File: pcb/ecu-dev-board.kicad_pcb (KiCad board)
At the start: 4 copper layers, 99.9 x 99.9 mm, 258 parts, among them IC201 MAX9924UAUB+, IC401 74HC14D-Q100,118, IC601 UCC28910DR, IC701 UCC27624DR, J101 MX23A18NF1, J102 39-30-1020, K501 Relay, Q201 MMBT2222A, Q501 MMBT2222A, Q502 MMBTA55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

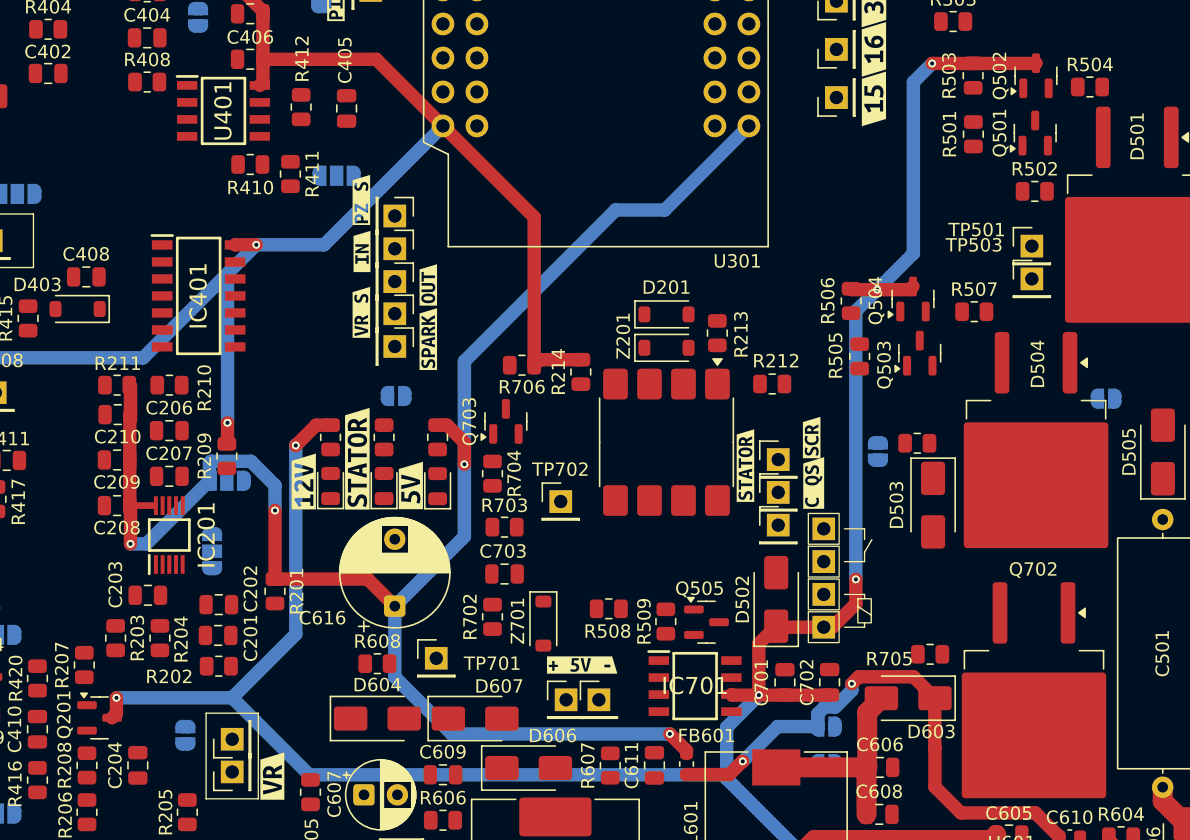
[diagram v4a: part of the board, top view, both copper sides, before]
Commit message: power aux connections
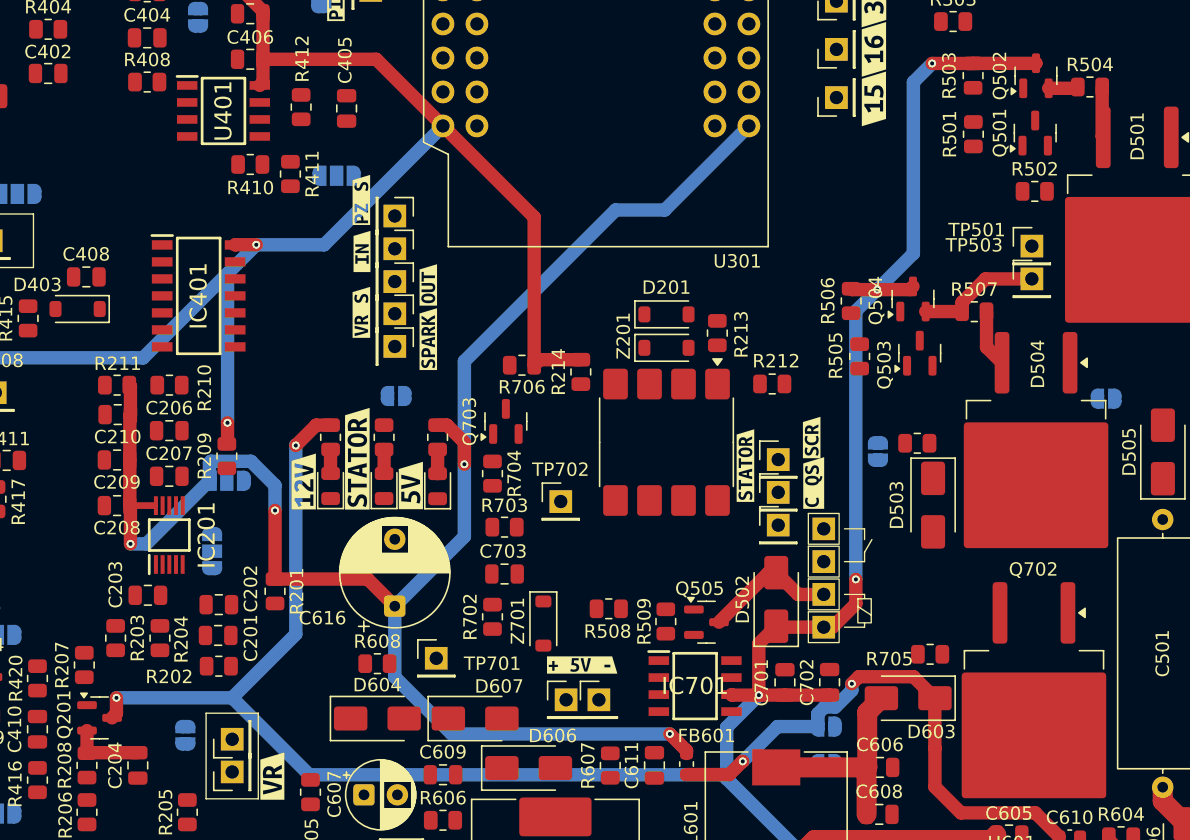
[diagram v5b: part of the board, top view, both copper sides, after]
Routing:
- net Net-(D502-A): track 0.00 -> 10.0 mm
- net Net-(Q504-E): track 0.00 -> 9.36 mm
- net Net-(Q201-E): track 0.00 -> 5.50 mm
- net Net-(D504-Pad3): track 0.00 -> 4.30 mm
- net Net-(D501-Pad3): track 0.00 -> 3.80 mm
- net Net-(Q502-E): track 0.00 -> 2.21 mm
- net Net-(D611-A): track 0.00 -> 1.80 mm
- net Net-(D610-A): track 0.00 -> 1.79 mm
- net Net-(D608-A): track 0.00 -> 1.79 mm
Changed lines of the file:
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@@
+	)
+	(segment
+		(start 168.3 101.1)
+		(end 168.3 102.7875)
+		(width 1)
+		(layer "F.Cu")
+		(net 9)
+	)
+	(segment
+		(start 172.1 102.75)
+		(end 168.3375 102.75)
+		(width 1)
+		(layer "F.Cu")
+		(net 9)
+	)
+	(segment
+		(start 168.3375 102.75)
+		(end 168.3 102.7875)
+		(width 1)
+		(layer "F.Cu")
+		(net 9)
 	)
 	(segment
@@
 	)
 	(segment
+		(start 244.155 56.695)
+		(end 244.235 56.775)
+		(width 1)
+		(layer "F.Cu")
+		(net 86)
+	)
+	(segment
+		(start 244.155 53.01)
+		(end 244.155 56.695)
+		(width 1)
+		(layer "F.Cu")
+		(net 86)
+	)
+	(segment
+		(start 221.425 90.925)
+		(end 219.8 89.3)
+		(width 1)
+		(layer "F.Cu")
+		(net 87)
+	)
+	(segment
+		(start 219.225 89.3)
+		(end 215.525 93)
+		(width 1)
+		(layer "F.Cu")
+		(net 87)
+	)
+	(segment
+		(start 219.8 89.3)
+		(end 219.225 89.3)
+		(width 1)
+		(layer "F.Cu")
+		(net 87)
+	)
+	(segment
+		(start 223.35 90.925)
+		(end 221.425 90.925)
+		(width 1)
+		(layer "F.Cu")
+		(net 87)
+	)
+	(segment
+		(start 235.5125 69.8)
+		(end 235.5125 72.4525)
+		(width 1)
+		(layer "F.Cu")
+		(net 91)
+	)
+	(segment
+		(start 235.5125 72.4525)
+		(end 236.675 73.615)
+		(width 1)
+		(layer "F.Cu")
+		(net 91)
+	)
+	(segment
+		(start 190.5 80.1)
+		(end 190.5 81.8875)
+		(width 1)
+		(layer "F.Cu")
+		(net 97)
+	)
+	(segment
+		(start 186.5 80.1)
+		(end 186.5 81.8875)
+		(width 1)
+		(layer "F.Cu")
+		(net 98)
+	)
+	(segment
+		(start 194.5 80.1)
+		(end 194.5 81.9)
+		(width 1)
+		(layer "F.Cu")
+		(net 99)
+	)
+	(segment
 		(start 211.852208 133.45)
 		(end 217.55 133.45)
@@
 	)
 	(segment
+		(start 240.1575 53.1075)
+		(end 242.2325 53.1075)
+		(width 1)
+		(layer "F.Cu")
+		(net 123)
+	)
+	(segment
+		(start 242.2325 53.1075)
+		(end 242.33 53.01)
+		(width 1)
+		(layer "F.Cu")
+		(net 123)
+	)
+	(segment
+		(start 235.4375 67.35)
+		(end 238.9 67.35)
+		(width 1)
+		(layer "F.Cu")
+		(net 126)
+	)
+	(segment
+		(start 233.6875 69.1)
+		(end 235.4375 67.35)
+		(width 1)
+		(layer "F.Cu")
+		(net 126)
+	)
+	(segment
+		(start 233.6875 69.8)
+		(end 233.6875 69.1)
+		(width 1)
+		(layer "F.Cu")
+		(net 126)
+	)
+	(segment
+		(start 233.675 69.7875)
+		(end 233.6875 69.8)
+		(width 1)
+		(layer "F.Cu")
+		(net 126)
+	)
+	(segment
+		(start 230.97 69.7875)
+		(end 233.675 69.7875)
+		(width 1)
+		(layer "F.Cu")
+		(net 126)
+	)
+	(segment

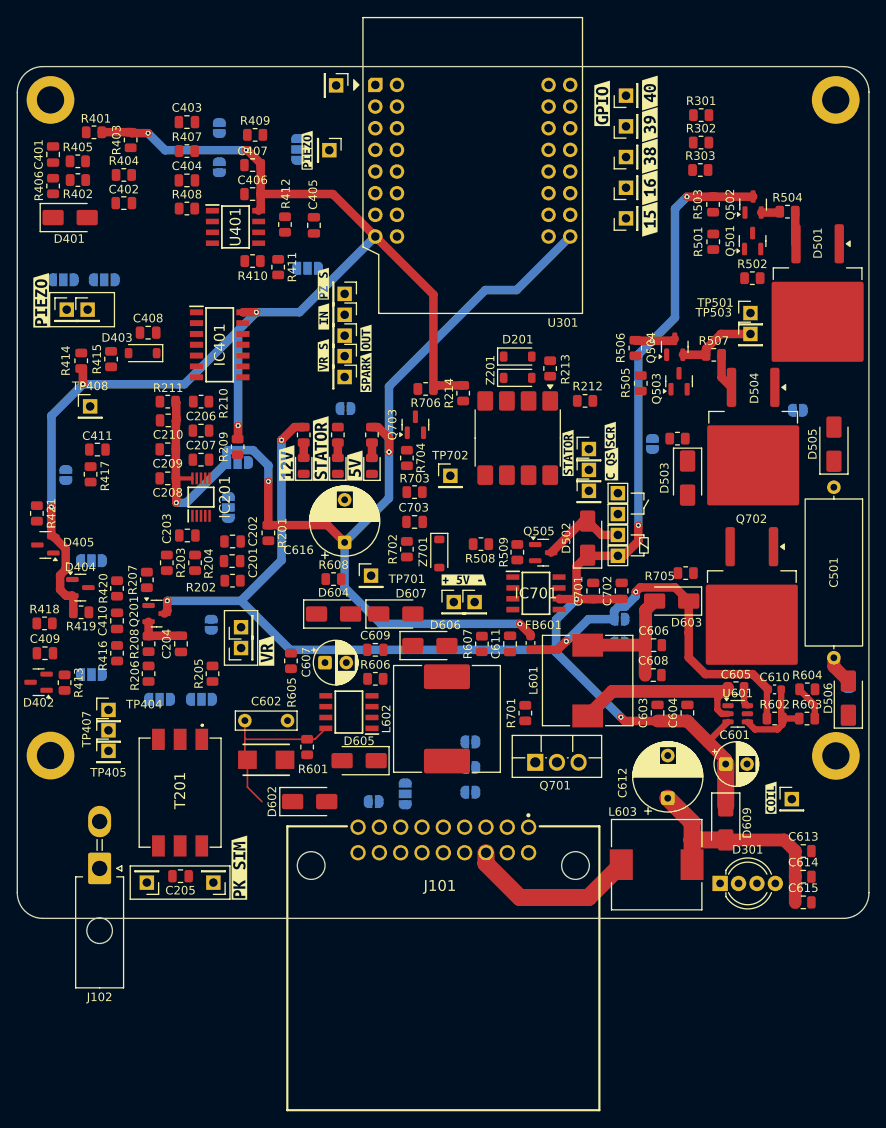
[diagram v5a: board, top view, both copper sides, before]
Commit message: routed batteryless from statort
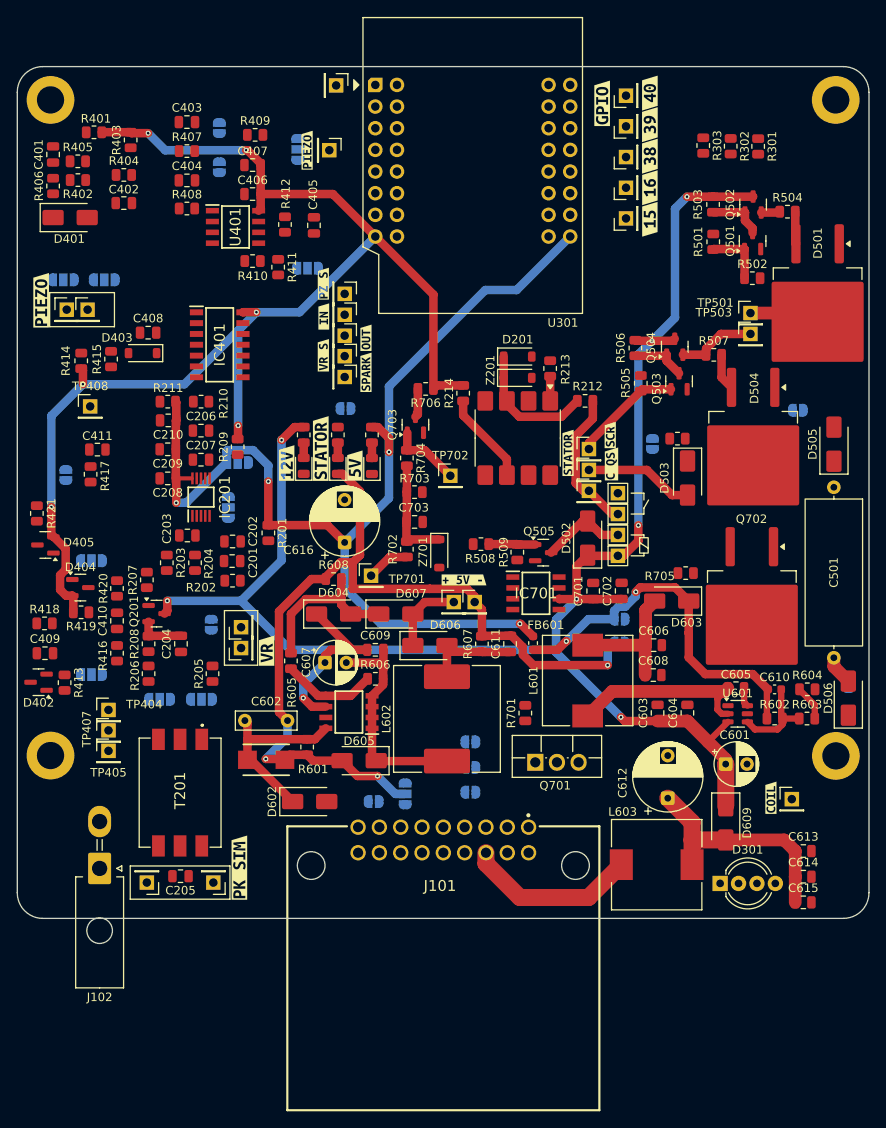
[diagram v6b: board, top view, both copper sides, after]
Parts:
- moved R301 7.62 mm to (239.8, 45.4), turned to -90 degrees
- moved R302 3.51 mm to (236.6, 45.3), turned to -90 degrees
- moved R303 2.89 mm to (233.4, 45.2), turned to -90 degrees
- moved FB601 0.30 mm to (213.4, 103.6)
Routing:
- net /PSU/RECT-: track 0.00 -> 103.0 mm, vias 0 -> 3
- net Net-(D605-K): track 0.00 -> 26.4 mm
- net Net-(D604-K): track 0.00 -> 20.2 mm, vias 0 -> 1
- net Net-(D604-A): track 0.00 -> 19.1 mm
- net COIL_QS: track 0.00 -> 16.9 mm
- net Net-(D201-K): track 0.00 -> 15.4 mm
- net Net-(Q503-B): track 0.00 -> 12.9 mm
- net Net-(C703-Pad1): track 0.00 -> 12.8 mm
- net STATOR: track 0.00 -> 12.8 mm
- net Net-(D606-A): track 0.00 -> 11.4 mm
- net Net-(IC601-VS): track 0.00 -> 11.1 mm
- net COIL_SPARK_OUT: track 0.00 -> 10.8 mm
- net Net-(D606-K): track 0.00 -> 9.08 mm
- net Net-(Q703-G): track 0.00 -> 8.41 mm
- net KILL_SWITCH: track 0.00 -> 8.30 mm
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
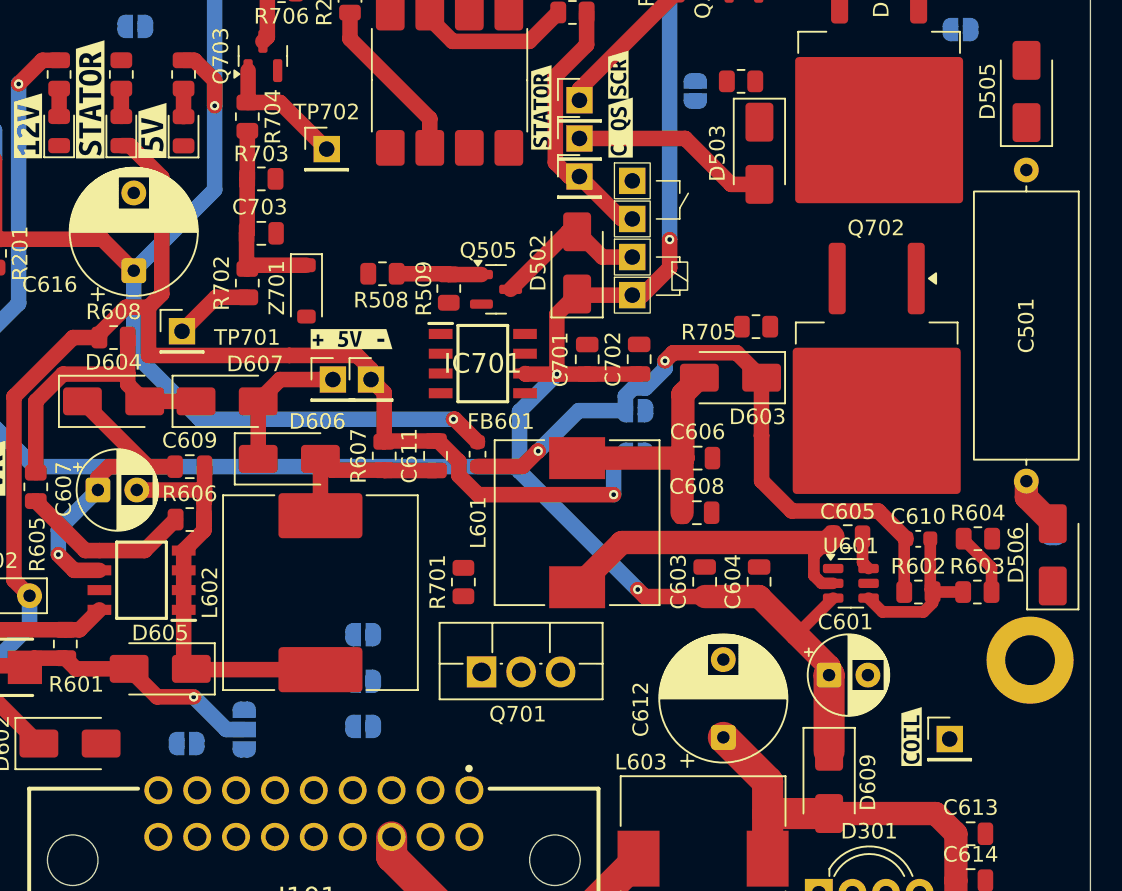
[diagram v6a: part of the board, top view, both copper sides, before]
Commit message: routed stator and CDI
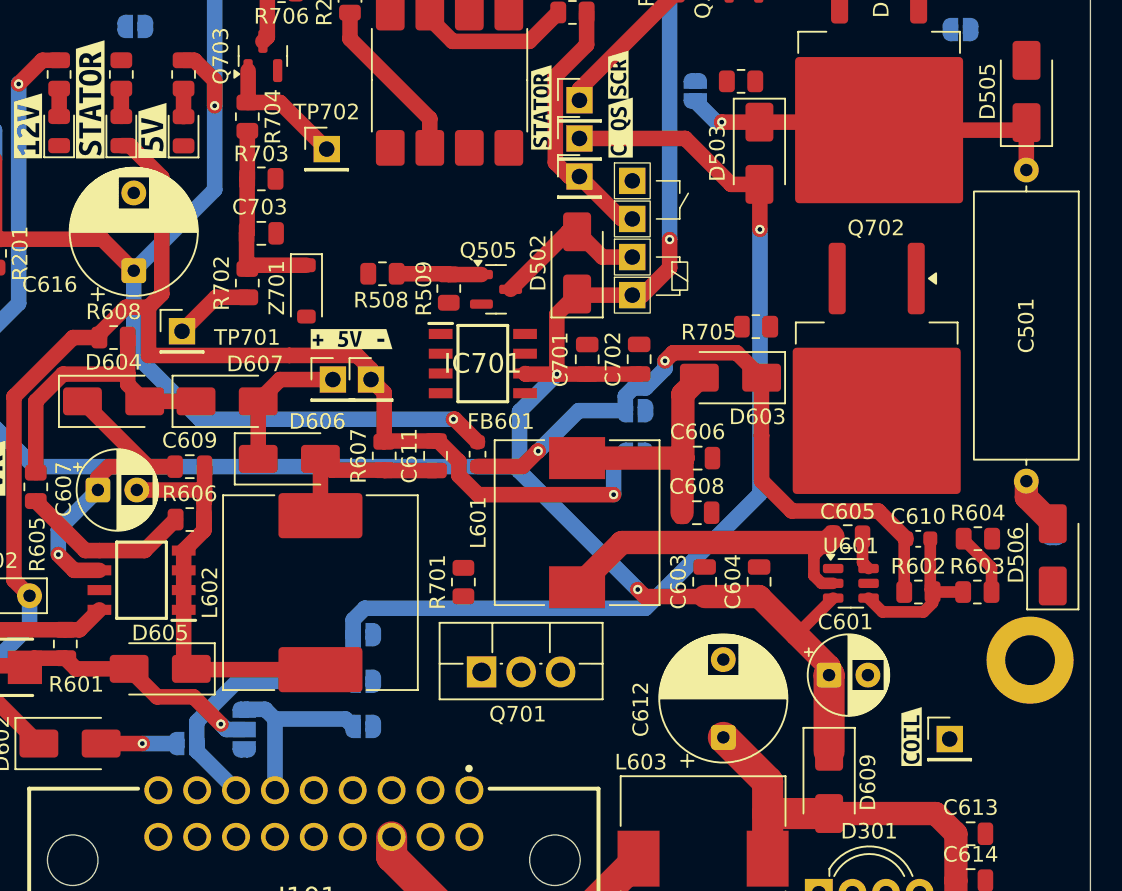
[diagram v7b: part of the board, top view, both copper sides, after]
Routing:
- net STATOR: track 12.8 -> 82.7 mm, vias 0 -> 1
- net Net-(D503-K): track 0.00 -> 25.3 mm, vias 0 -> 1
- net STATOR_2: track 0.00 -> 12.0 mm
- net Net-(D602-A): track 0.00 -> 4.85 mm, vias 0 -> 1

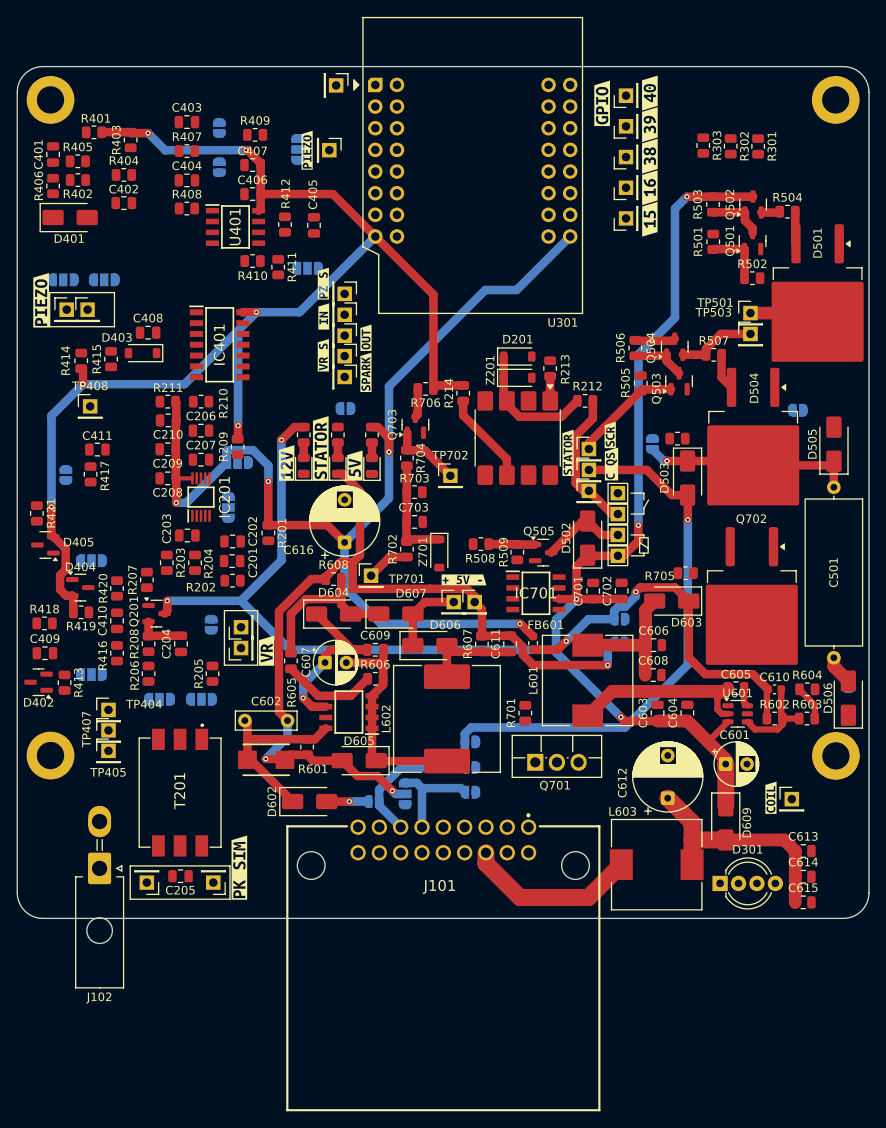
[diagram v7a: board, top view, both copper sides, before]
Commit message: made some traces bigger and routed partially the TCI
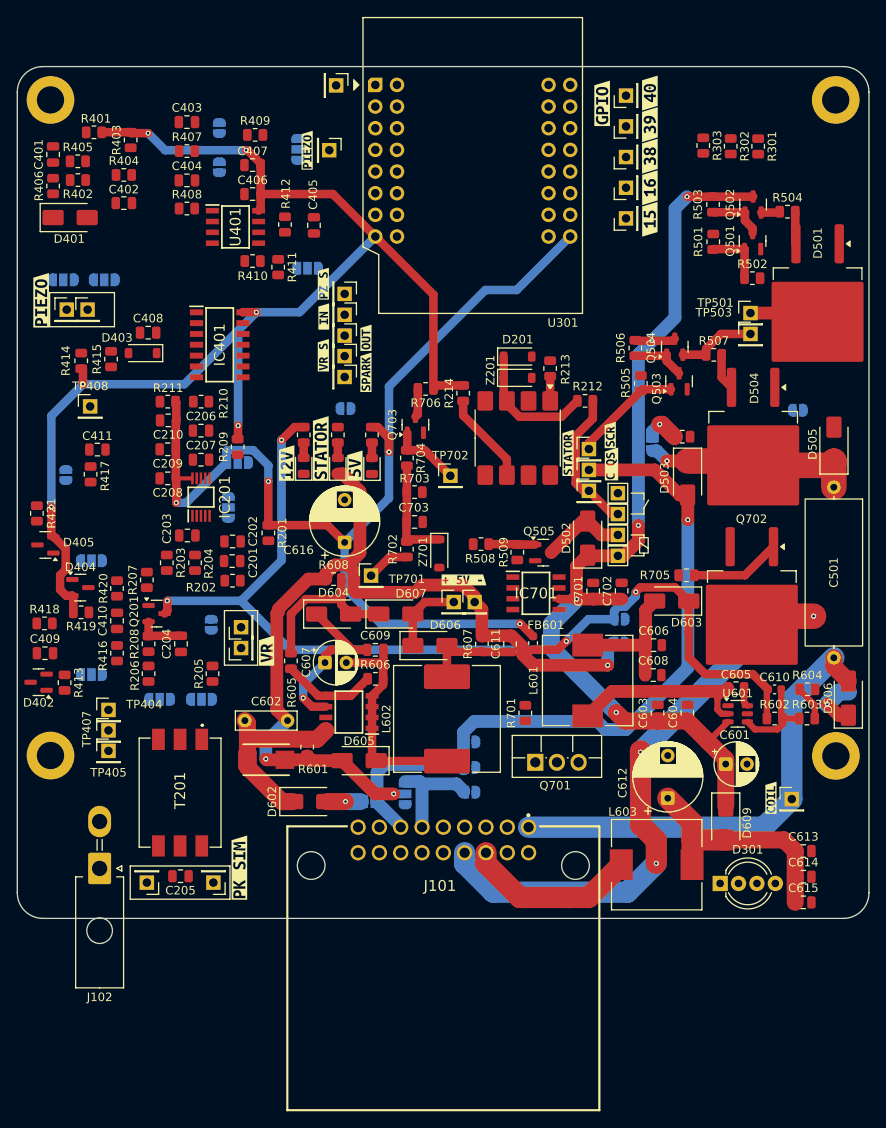
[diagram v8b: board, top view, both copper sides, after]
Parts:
- moved R510 0.61 mm to (230.9, 79.4), turned to 180 degrees
- moved JP601 0.50 mm to (194.2, 122.2)
- moved R705 0.26 mm to (231.4, 95.7)
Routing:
- net T_COIL: track 5.11 -> 80.2 mm, vias 0 -> 3
- net COIL: track 3.44 -> 54.3 mm
- net Net-(Q702-Pad1): track 0.00 -> 10.7 mm
- net Net-(D506-K): track 0.00 -> 6.10 mm, vias 0 -> 1
- net Net-(JP502-A): track 0.00 -> 4.10 mm, vias 0 -> 1
- net STATOR: track 82.7 -> 85.5 mm
- net /PSU/RECT-: track 103.0 -> 104.6 mm
- net Net-(D602-A): track 4.85 -> 3.94 mm
- net /PSU/RECT+: track 22.2 -> 23.0 mm
